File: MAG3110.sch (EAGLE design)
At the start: 4 parts

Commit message: porzadki w plikach
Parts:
- removed AKC+GYRO: LSM330DLC, sensors-akc_zyr:LSM330DLC
- added C4: 100n, rcl:C-EUC0805
- added C5: 1uF, rcl:CPOL-EUSMCA
- added MAG3110: MAG3110, sparkfun-sensors (2):MAG3110
- added R1?, R2?: 4.7k, rcl:R-EU_R0805
- C1, C2: value (none) -> 100n; device resistor:C-EUC0805 -> rcl:C-EUC0805
- C3: value (none) -> 100n; device rcl:CPOL-EUSMCA -> rcl:C-EUC0805
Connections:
- removed net INT_AKC: AKC+GYRO.INT1_A
- removed net INT_GYRO: AKC+GYRO.INT1_G
- removed net N$1: AKC+GYRO.CAP, C2.1
- new net INT_MAG: MAG3110.INT1
- new net N$2: C3.2, MAG3110.CAP-R
- new net N$3: C1.2, MAG3110.CAP-A
- net 3.3V: now also C2.1, C4.1, C5.+, MAG3110.VDD, MAG3110.VDDIO, R1?.2, R2?.2; no longer AKC+GYRO.!CS_A, AKC+GYRO.!CS_G, AKC+GYRO.VDD, AKC+GYRO.VDD_IO, C1.2, C3.+
- net GND: now also C3.1, C4.2, C5.-, MAG3110.GND@10, MAG3110.GND@5; no longer AKC+GYRO.DEN_G, AKC+GYRO.SDO_A, AKC+GYRO.SDO_G, AKC+GYRO.VSS, C3.-
- net SCL: now also MAG3110.SCL, R2?.1; no longer AKC+GYRO.SCL
- net SDA: now also MAG3110.SDA, R1?.1; no longer AKC+GYRO.SDA
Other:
- note added: "MAG3110 Magnetometer"
- moved on the sheet: C1, C2

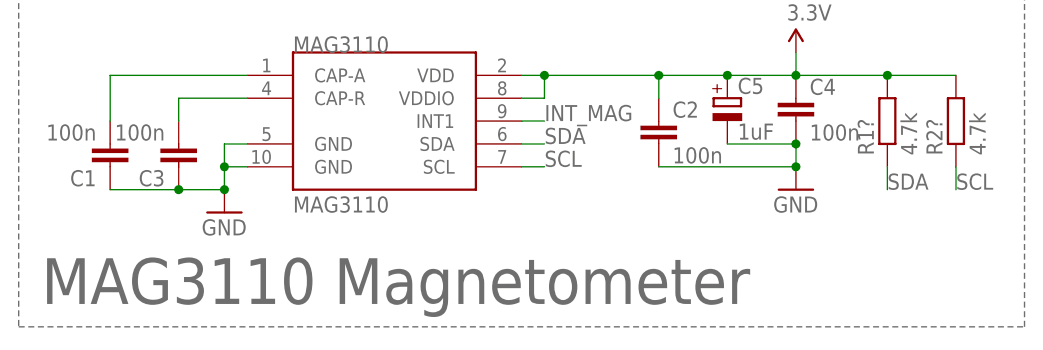
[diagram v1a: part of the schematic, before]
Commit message: dodane obwodki z nazwami dla poszczegolnych elementow
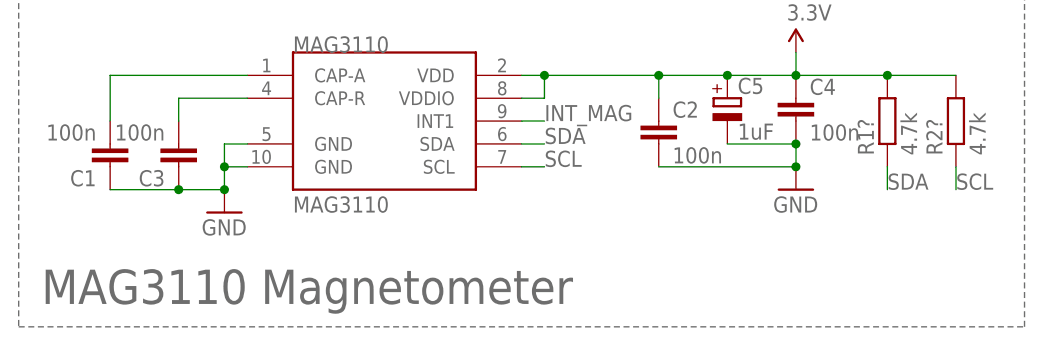
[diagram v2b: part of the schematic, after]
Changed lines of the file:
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@@
 <wire x1="111.76" y1="38.1" x2="0" y2="38.1" width="0.1524" layer="95" style="shortdash"/>
 <wire x1="0" y1="38.1" x2="0" y2="0" width="0.1524" layer="95" style="shortdash"/>
-<text x="2.54" y="2.54" size="5.08" layer="95">MAG3110 Magnetometer</text>
+<text x="2.54" y="2.54" size="3.81" layer="95">MAG3110 Magnetometer</text>
 </plain>
 <instances>
